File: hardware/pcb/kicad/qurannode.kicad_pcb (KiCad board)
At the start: 4 copper layers, 62.8 x 150 mm, 87 parts, among them J1 USB-C-16P, J2 microSD, J3 LCD_HDR_1x14, J4 SPK_JST_PH2, J5 BATT_JST_PH2, J6 TRS_3.5, Q1 2N7002, Q2 AO3401A_PFET, Q3 2N7002_NFET, SW1 NAV_5WAY, SW2 RST, SW3 BOOT, U1 ESP32-S3-WROOM-1, U2 PCM5102A, U3 PAM8302A, U4 TP4056, U5 TPS63020, U6 USBLC6-2SC6, U7 DW01A, U8 FS8205A

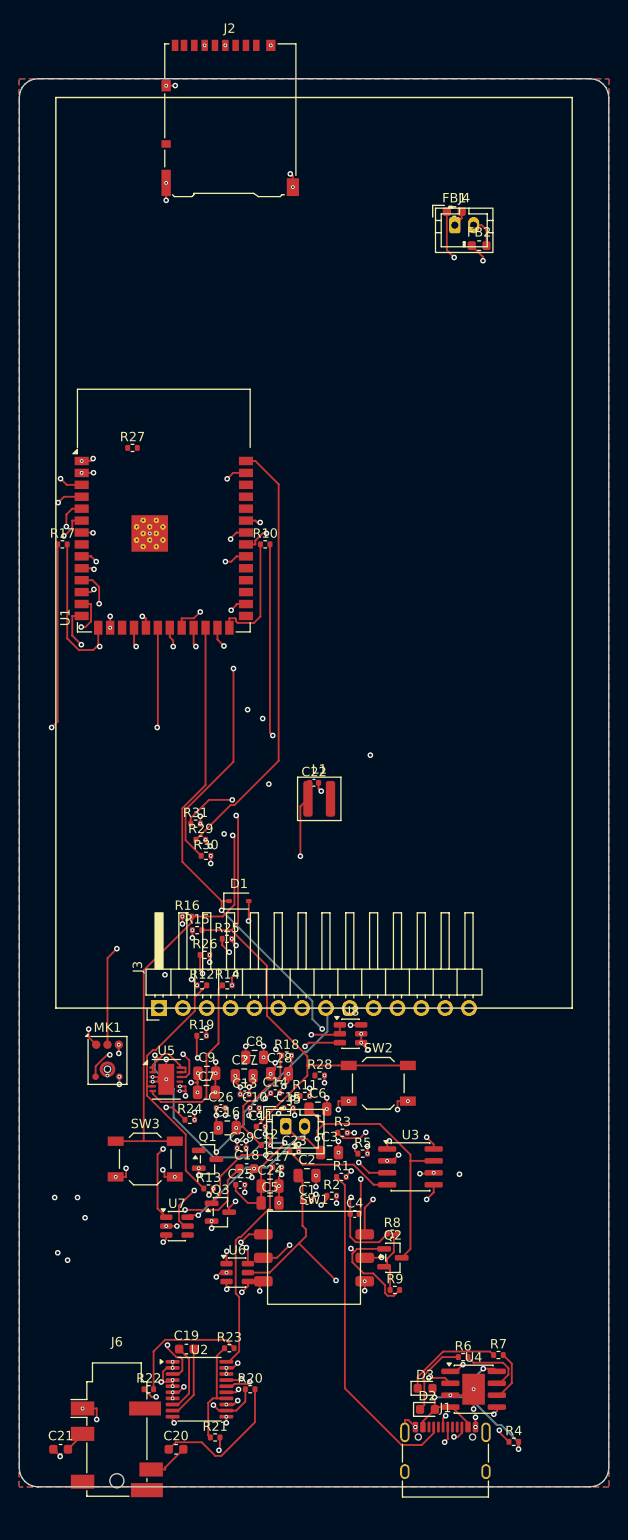
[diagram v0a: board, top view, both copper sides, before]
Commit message: PCB: clean up to 0 electrical DRC faults + handoff doc
Routed board cleaned from 546 DRC / 33 shorts down to 117 DRC / 0 electrical
faults (0 shorts, 0 clearance, 0 mask bridges), ~94% routed (19 nets left for
the interactive router). Remaining DRC is footprint-inherent (edge connectors,
ESP32 thermal pad, mounting holes) + cosmetic (silk-over-pad JLC auto-clips,
tight courtyards) -- all fab-acceptable.

What fixed the shorts:
- Removed the fanout via-in-pads (they bridged neighbour pads -> 31 shorts).
- half_ext now measures pad EDGES (pos +/- size/2) not centres, so big-pad
  parts (the inductor) can't overlap -> killed the last short.
- JLC-friendly design rules, refs moved to F.Fab, GND pour inset from the edge,
  solid zone connections; new finalize.py (import SES + pours + fill).

HANDOFF.md: self-contained doc for a fresh instance to finish the board --
the headless toolchain (mounted KiCad DMG + bundled python, FreeRouting, SKiDL
venv), the regenerate pipeline, the race/gotcha list, remaining work, firmware
TODO, and the verify-before-fab checklist.

Co-Authored-By: Claude Opus 4.8 (1M context) <noreply@anthropic.com>
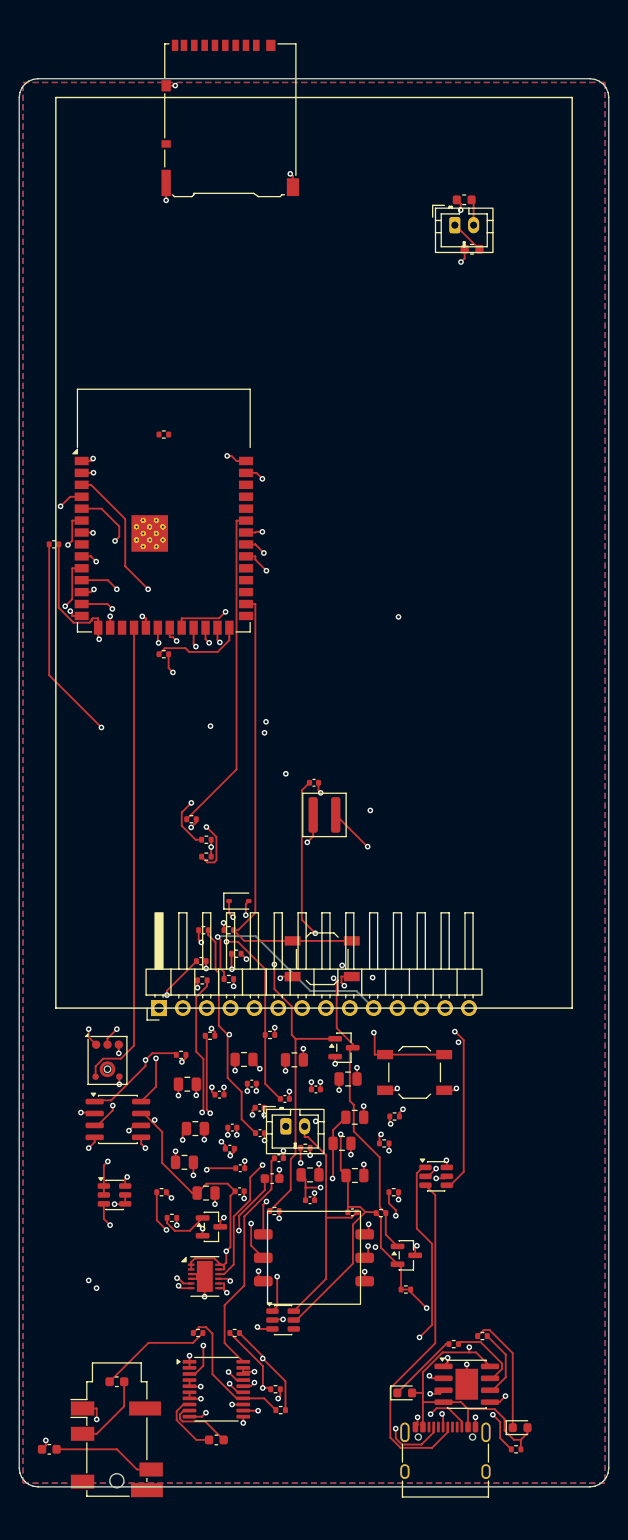
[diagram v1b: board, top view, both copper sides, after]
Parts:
- moved U3 31.6 mm to (10.5, 110.9)
- moved U8 30.4 mm to (10.2, 118.9)
- moved SW3 28.5 mm to (32.3, 93.7)
- moved U6 23.5 mm to (44.4, 116.9)
- moved Q3 21.9 mm to (34.6, 103.2)
- moved R28 21.9 mm to (16.3, 121.3)
- moved R5 21.8 mm to (15.2, 118.6)
- moved U5 21.4 mm to (19.8, 127.6)
- moved R13 19.3 mm to (38.9, 113.4)
- moved R10 15.9 mm to (15.4, 61.3)
- moved U7 15.1 mm to (28.1, 132.2)
- moved C9 15.1 mm to (35.0, 106.6)
- moved C20 13.5 mm to (3.20, 146.0)
- moved C8 13.5 mm to (17.6, 115.4)
- moved R11 12.7 mm to (27.2, 120.6)
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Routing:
- net N$14: track 0.00 -> 67.0 mm, vias 0 -> 3
- net AIN: track 13.5 -> 74.8 mm, vias 0 -> 2
- net AMP_EN: track 98.5 -> 66.8 mm, vias 3 -> 2
- net N$15: track 27.6 -> 56.9 mm, vias 0 -> 3
- net N$27: track 106.5 -> 130.0 mm, vias 2 -> 3
- net IO0: track 71.2 -> 50.0 mm, vias 2 -> 0
- net PG: track 19.2 -> 38.3 mm, vias 0 -> 2
- net VBAT: track 80.2 -> 62.3 mm
- net NAV_UP: track 86.3 -> 102.8 mm, vias 4 -> 2
- net N$13: track 37.2 -> 53.4 mm
- net EN: track 99.1 -> 114.8 mm, vias 2 -> 3
- net N$22: track 15.1 -> 28.8 mm, vias 0 -> 2
- net VBAT_SENSE: track 85.8 -> 72.1 mm, vias 3 -> 2
- net PWR_G: track 62.4 -> 49.0 mm, vias 3 -> 2
- net N$26: track 101.7 -> 114.4 mm, vias 2 -> 3
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
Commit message: PCB: finish routing — 0 unconnected, 0 electrical DRC faults, fab outputs
- J2 microSD + J6 jack: pads were off-board with openings facing INTO the
  board; rotate 180deg + extent-aware clamp (copper stays on-board, jack
  barrel may overhang)
- Placement occupancy = pads UNION courtyard: parts no longer land under the
  WROOM module's padless antenna end (this is what made DISP_BL/BL_G/SD
  unroutable); all 22 courtyard overlaps gone
- In2 +3V3 plane: 0.2 clearance / 0.15 min-width so via fences don't split it
- heal_plane.py: new step (e2) — 2 B.Cu island bridges + INMP441 3V3 fanout,
  the 3 gaps FreeRouting can't see
- qurannode.ses force-added: FR output varies across versions; heal coords
  and the routed board are pinned to this session file
- fab/: Gerbers (11 layers) + Excellon drill + zip, kicad-cli export
- Remaining 31 DRC are footprint-inherent or silk-cosmetic (see HANDOFF §0)

Co-Authored-By: Claude Fable 5 <noreply@anthropic.com>
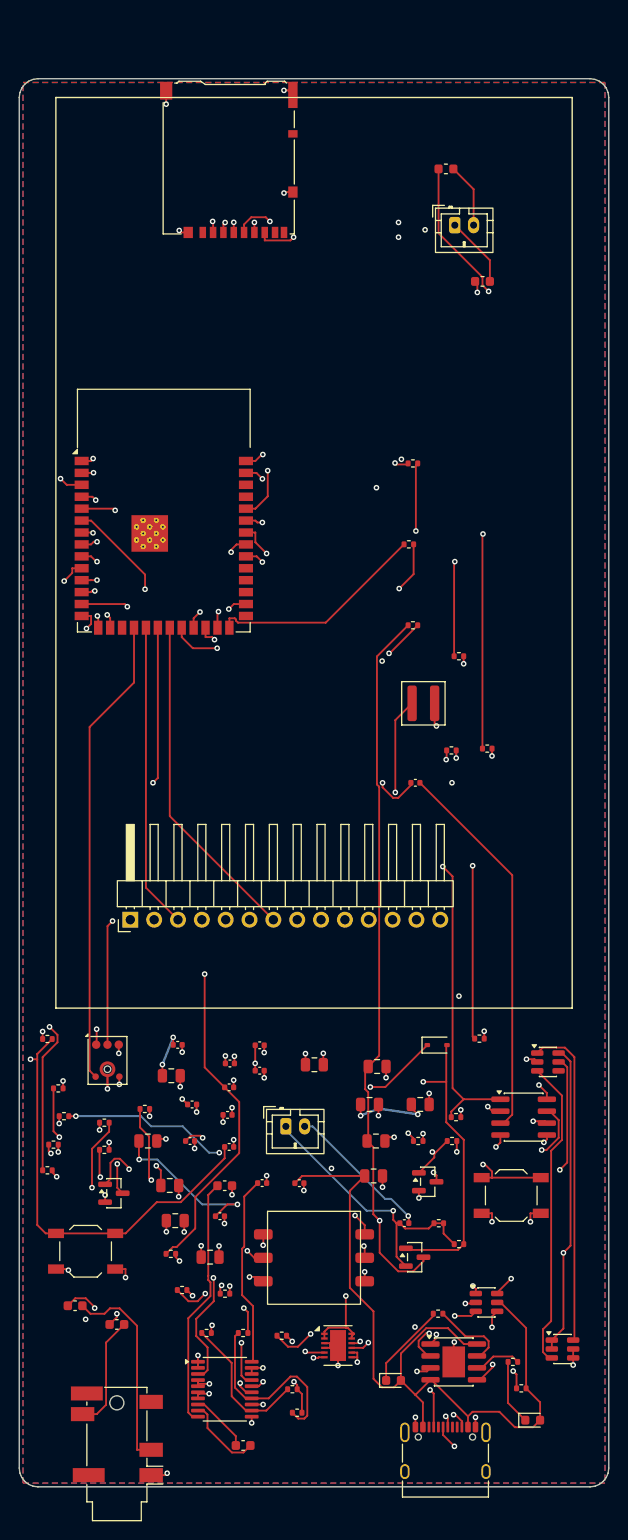
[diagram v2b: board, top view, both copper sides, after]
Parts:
- moved U8 50.5 mm to (57.9, 135.3)
- moved U3 43.2 mm to (53.7, 110.6)
- moved SW2 39.9 mm to (7.07, 124.9)
- moved U7 39.4 mm to (56.3, 104.7)
- moved R17 39.2 mm to (41.9, 58.2)
- moved R31 38.6 mm to (49.0, 102.3)
- moved R30 34.3 mm to (46.8, 61.5)
- moved SW3 32.3 mm to (52.4, 119.0)
- moved R25 31.5 mm to (46.0, 71.6)
- moved R29 31.5 mm to (49.9, 71.4)
- moved R3 31.1 mm to (9.06, 114.1)
- moved R28 30.9 mm to (46.1, 113.2)
- moved R24 30.0 mm to (46.5, 110.6)
- moved Q3 29.0 mm to (10.1, 118.7)
- moved R10 28.6 mm to (41.5, 49.6)
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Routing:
- net SD_MISO: track 35.0 -> 119.3 mm, vias 0 -> 5
- net BL_G: track 5.24 -> 79.3 mm, vias 0 -> 2
- net IO0: track 50.0 -> 115.7 mm, vias 0 -> 4
- net SD_CLK: track 0.00 -> 64.1 mm, vias 0 -> 4
- net VBAT_SENSE: track 72.1 -> 127.5 mm, vias 2 -> 3
- net SD_CS: track 46.4 -> 95.4 mm, vias 2 -> 3
- net SD_MOSI: track 47.7 -> 95.9 mm, vias 2 -> 4
- net VBAT: track 62.3 -> 103.1 mm, vias 3 -> 4
- net DISP_BL: track 0.00 -> 38.5 mm, vias 0 -> 2
- net TOUCH_SCL: track 71.9 -> 103.3 mm
- net HOLD_G: track 72.0 -> 102.1 mm
- net NAV_MID: track 80.4 -> 106.5 mm, vias 4 -> 3
- net N$26: track 114.4 -> 90.3 mm, vias 3 -> 2
- net AMP_EN: track 66.8 -> 90.8 mm
- net NAV_UP: track 102.8 -> 80.3 mm
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
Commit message: PCB respin v2: fix verified pinout bugs, JLCPCB-ready fab + assembly
Pre-fab datasheet audit of every IC caught several wrong pinouts/footprints
that would have failed a fab run. Board re-placed, re-routed, healed to
0 unconnected / 0 electrical DRC. CPL + JLCPCB BOM regenerated; all parts are
in-stock LCSC # with matching footprints.

Fixes (datasheet-verified):
- PCM5102A (U2): pinout was entered reversed (19/20 pins wrong) -> SLAS859C; C107671
- PAM8302A (U3): VDD/GND + VO+/- swapped, pin2(NC) grounded -> MSOP-8 land; C113367
- USBLC6 (U6): D+/D- cross-wired across the two TVS lines -> 1&6=D+, 3&4=D-;
  both Type-C sides tied for orientation-independent USB data
- TPS63020 (U5): real DSJ is VSON-14 0.5mm, board had 12-pad DFN ->
  custom qurannode:TPS63020_DSJ_VSON14 footprint; C15483
- Inductor (L1): part 4.4x4.2 vs 4x4 land (0.3mm overlap) ->
  custom qurannode:MWSA0402S footprint from datasheet; C408334
- Mic (MK1): INMP441 out of stock -> ICS-43434 (C5656610), new land
- Cell protection (DW01A+FS8205): mis-wired + redundant with LP603449 PCM -> removed
- SD_MISO pull-up: pinned near J2 so the net routes (build_board.py)

Deliverables in fab/: gerbers zip, drill, qurannode-cpl.csv (73 SMT parts),
qurannode-bom-jlc.csv (29 lines), ASSEMBLY-NOTES.md. Hand-solder parts (module,
connectors, nav, RST/BOOT) excluded from the SMT CPL/BOM.

Co-Authored-By: Claude Opus 4.8 (1M context) <noreply@anthropic.com>
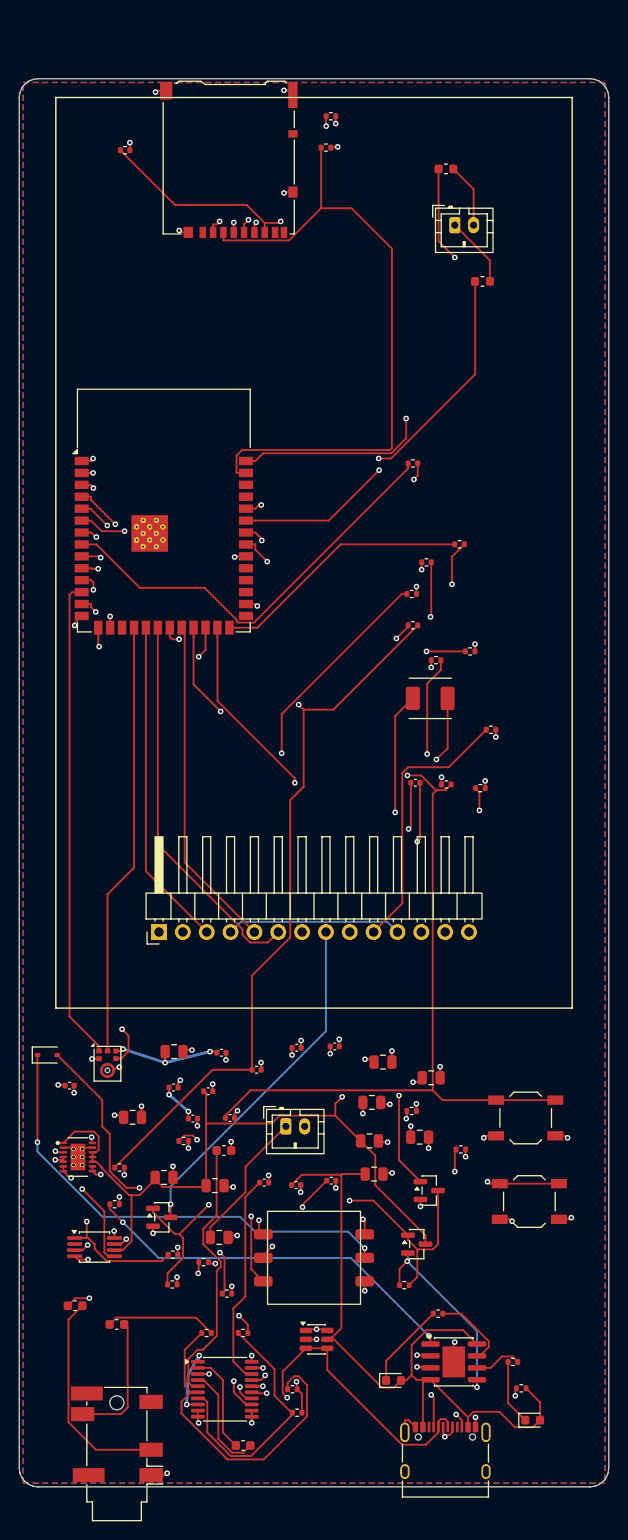
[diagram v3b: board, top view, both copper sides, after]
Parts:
- removed C29: 100n, C_0402_1005Metric
- removed R31: 10k, R_0402_1005Metric
- removed U7: DW01A, SOT-23-6
- removed U8: FS8205A, SOT-23-6
- C10: value 100n -> 1u
- C11: value 1u -> 100n
- C15, C26, C4: value 100n -> 10u; footprint C_0402_1005Metric -> C_0805_2012Metric
- C16: value 10u -> 1u; footprint C_0805_2012Metric -> C_0402_1005Metric
- C17: value 1u -> 2u2; footprint C_0402_1005Metric -> C_0603_1608Metric
- C21: value 2u2 -> 470n; footprint C_0603_1608Metric -> C_0402_1005Metric
- C23: value 470n -> 10u; footprint C_0402_1005Metric -> C_0805_2012Metric
- C24, C28: value 10u -> 100n; footprint C_0805_2012Metric -> C_0402_1005Metric
- C6: value 10u -> 22u
- C9: value 22u -> 100n; footprint C_0805_2012Metric -> C_0402_1005Metric
- L1: footprint L_Abracon_ASPIAIG-F4020 -> MWSA0402S
- MK1: value INMP441 -> ICS-43434; footprint Knowles_LGA-6_4.72x3.76mm -> InvenSense_ICS-43434-6_3.5x2.65mm
- R10, R16: value 10k -> 100k
- R11: value 100k -> 560k
- R12: value 560k -> 100k
- R14, R18, R9: value 100k -> 10k
- R19: value 10k -> 100R
- R21: value 100R -> 20k
- R23: value 20k -> 100k
- R24: value 100k -> 4k7
- R26: value 4k7 -> 100R
- R27: value 100R -> 10k
- R8: value 100R -> 100k
- U3: footprint SOIC-8_3.9x4.9mm_P1.27mm -> MSOP-8_3x3mm_P0.65mm
- U5: footprint DFN-12-1EP_3x4mm_P0.5mm_EP1.7x3.3mm -> TPS63020_DSJ_VSON14
- moved R28 109.9 mm to (33.2, 4.00)
- moved R27 91.1 mm to (16.3, 128.4)
- moved R26 84.8 mm to (41.9, 41.0)
- moved R13 77.1 mm to (41.8, 54.9)
- moved R9 74.5 mm to (46.9, 49.6)
- moved R10 67.9 mm to (17.5, 113.1)
- moved C21 66.5 mm to (42.2, 75.0)
- moved R29 66.3 mm to (32.7, 7.34)
- moved R17 65.7 mm to (10.7, 116.0)
- moved R15 64.9 mm to (43.4, 51.5)
- moved R30 64.6 mm to (11.3, 7.62)
- moved R16 64.2 mm to (41.9, 58.2)
- moved R18 59.6 mm to (49.1, 75.6)
- moved R14 52.5 mm to (45.5, 75.2)
- moved R11 51.3 mm to (44.4, 61.9)
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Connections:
- C10 pad 1: +3V3 -> EN
- C11 pad 1: EN -> VBAT_SENSE
- C12 pad 1: VBAT_SENSE -> +3V3
- C16 pad 1: +3V3 -> N$11
- C17 pad 1: N$17 (its old number) -> N$12
- C18 pad 1: N$18 -> N$13
- C18 pad 2: GND -> N$14
- C19 pad 1: N$19 -> N$16
- C19 pad 2: N$20 -> HP_L
- C20 pad 2: HP_L -> HP_R
- C21 pad 1: N$23 -> AIN
- C21 pad 2: HP_R -> N$18
- C22 pad 1: AIN -> N$19
- C22 pad 2: N$24 -> GND
- C23 pad 1: N$25 -> VSYS
- C25 pad 1: VSYS -> +3V3
- C4 pad 1: VBAT -> VSYS
- C4 pad 2: N$9 -> GND
- C6 pad 1: VSYS -> +3V3
- FB1 pad 1: N$26 -> N$20
- FB2 pad 1: N$27 -> N$21
- J1 pad A6: N$3 (its old number) -> USB_DP
- J1 pad A7: N$4 (its old number) -> USB_DM
- J1 pad B6: (no net) -> USB_DP
- J1 pad B7: (no net) -> USB_DM
- J5 pad 2: N$9 -> GND
- L1 pad 1: N$13 -> N$7
- L1 pad 2: N$14 -> N$8
- MK1 pad 1: MIC_SCK -> MIC_WS
- MK1 pad 2: MIC_SD -> GND
- MK1 pad 3: +3V3 -> GND
- MK1 pad 4: GND -> MIC_SCK
- MK1 pad 5: GND -> +3V3
- MK1 pad 6: MIC_WS -> MIC_SD
- R10 pad 1: PWR_HOLD -> HOLD_G
- R10 pad 2: HOLD_G -> GND
- R11 pad 1: HOLD_G -> +3V3
- R11 pad 2: GND -> N$9
- R12 pad 1: +3V3 -> N$9
- R12 pad 2: N$15 -> GND
- R13 pad 1: N$15 -> PG
- R13 pad 2: GND -> +3V3
- R14 pad 1: PG -> +3V3
- R14 pad 2: +3V3 -> EN
- R15 pad 2: EN -> IO0
- R16 pad 1: +3V3 -> VSYS
- R16 pad 2: IO0 -> VBAT_SENSE
- R17 pad 1: VSYS -> VBAT_SENSE
- R17 pad 2: VBAT_SENSE -> GND
- R18 pad 1: VBAT_SENSE -> N$15
- R18 pad 2: GND -> +3V3
- R19 pad 1: N$21 -> OUTL
- R19 pad 2: +3V3 -> N$16
- R20 pad 1: OUTL -> OUTR
- R21 pad 1: OUTR -> OUTL
- R21 pad 2: N$23 -> AIN
- R22 pad 1: OUTL -> OUTR
- R23 pad 1: OUTR -> AMP_EN
- R23 pad 2: AIN -> GND
- R24 pad 1: AMP_EN -> TOUCH_SDA
- R24 pad 2: GND -> +3V3
- R25 pad 1: TOUCH_SDA -> TOUCH_SCL
- R26 pad 1: TOUCH_SCL -> DISP_BL
- R26 pad 2: +3V3 -> BL_G
- R27 pad 1: DISP_BL -> BL_G
- R27 pad 2: BL_G -> GND
- R28 pad 1: BL_G -> SD_CS
- R28 pad 2: GND -> +3V3
- R29 pad 1: SD_CS -> SD_MOSI
- R30 pad 1: SD_MOSI -> SD_MISO
- R8 pad 2: VBAT -> PWR_G
- R9 pad 1: VBAT -> PWR_HOLD
- R9 pad 2: PWR_G -> HOLD_G
- U2 pad 1: GND -> +3V3
- U2 pad 10: N$18 -> GND
- U2 pad 12: OUTL -> GND
- U2 pad 13: +3V3 -> I2S_BCK
- U2 pad 14: OUTR -> I2S_DATA
- U2 pad 16: I2S_BCK -> GND
- U2 pad 17: I2S_DATA -> N$15
- U2 pad 18: GND -> N$11
- U2 pad 2: GND -> N$13
- U2 pad 20: N$17 (its old number) -> +3V3
- U2 pad 3: N$21 -> GND
- U2 pad 4: GND -> N$14
- U2 pad 5: GND -> N$12
- U2 pad 6: +3V3 -> OUTL
- U2 pad 7: +3V3 -> OUTR
- U2 pad 8: N$19 -> +3V3
- U2 pad 9: N$20 -> GND
- U3 pad 2: GND -> (no net)
- U3 pad 3: N$24 -> N$18
- U3 pad 4: N$25 -> N$19
- U3 pad 5: N$27 -> N$20
- U3 pad 6: GND -> VSYS
- U3 pad 7: VSYS -> GND
- U3 pad 8: N$26 -> N$21
- U5 pad 10: N$13 -> VSYS
- U5 pad 2: VSYS -> GND
- U5 pad 3: GND -> N$9
- U5 pad 4: GND -> +3V3
- U5 pad 5: N$15 -> +3V3
- U5 pad 6: PG -> N$8
- U5 pad 7: +3V3 -> N$8
- U5 pad 8: +3V3 -> N$7
- U5 pad 9: N$14 -> N$7
- U6 pad 1: N$3 (its old number) -> USB_DP
- U6 pad 3: N$4 (its old number) -> USB_DM
- U6 pad 4: USB_DP -> USB_DM
- U6 pad 6: USB_DM -> USB_DP
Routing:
- net N$20: track 8.58 -> 138.2 mm, vias 0 -> 2
- net N$21: track 36.2 -> 149.2 mm
- net N$27: track 109.3 -> 0.00 mm, vias 2 -> 0
- net N$26: track 90.3 -> 0.00 mm, vias 2 -> 0
- net N$8: track 0.00 -> 70.8 mm, vias 0 -> 2
- net N$7: track 0.00 -> 67.4 mm, vias 0 -> 2
- net N$14: track 74.5 -> 11.8 mm, vias 2 -> 0
- net N$13: track 71.2 -> 10.7 mm, vias 2 -> 0
- net VBAT: track 103.1 -> 56.0 mm, vias 4 -> 2
- net SD_MISO: track 119.3 -> 75.0 mm, vias 5 -> 2
- net N$24: track 41.1 -> 0.00 mm
- net N$18: track 26.9 -> 65.8 mm, vias 0 -> 2
- net N$9: track 67.0 -> 103.9 mm, vias 2 -> 3
- net N$15: track 41.6 -> 77.7 mm, vias 3 -> 2
- net N$25: track 35.3 -> 0.00 mm, vias 2 -> 0
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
